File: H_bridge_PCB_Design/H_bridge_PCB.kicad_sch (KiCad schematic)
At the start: 6 parts, among them U1 ESP32-WROOM-32

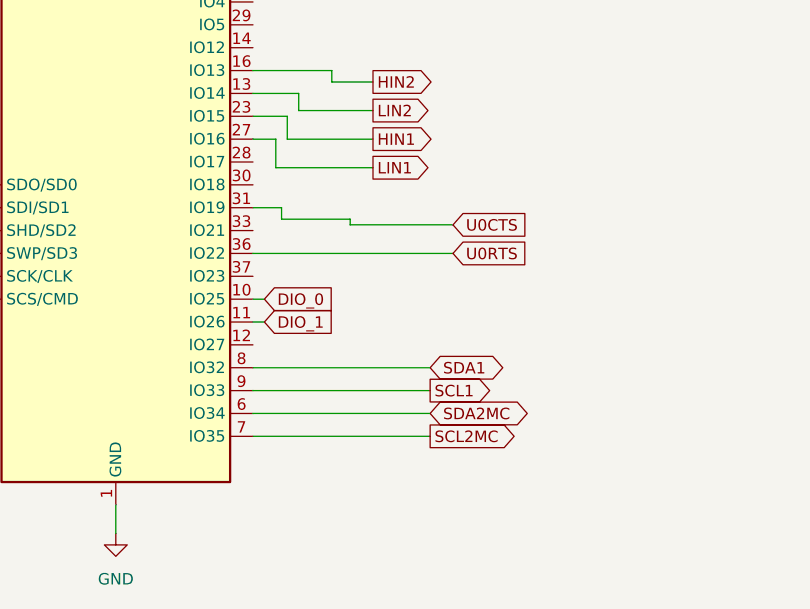
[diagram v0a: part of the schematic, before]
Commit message: Added picutres for bipolar and unipolar, changed pins for I2C-2
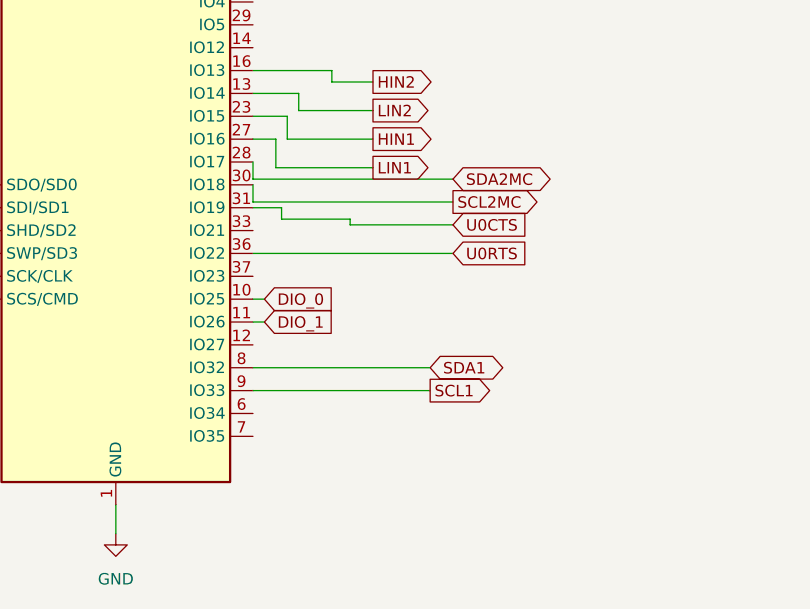
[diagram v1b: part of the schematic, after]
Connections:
- net SCL2MC: now also U1.30 (IO18); no longer U1.7 (IO35)
- net SDA2MC: now also U1.28 (IO17); no longer U1.6 (IO34)
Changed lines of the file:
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@@
+	(wire
+		(pts
+			(xy 198.12 215.9) (xy 198.12 213.995)
+		)
+		(stroke
+			(width 0)
+			(type default)
+		)
+	)
 	(wire
 		(pts
@@
 	(wire
 		(pts
-			(xy 198.12 241.935) (xy 217.805 241.935)
-		)
-		(stroke
-			(width 0)
-			(type default)
-		)
-	)
-	(wire
-		(pts
 			(xy 171.45 175.26) (xy 171.45 173.355)
 		)
@@
 	(wire
 		(pts
+			(xy 198.12 213.36) (xy 220.345 213.36)
+		)
+		(stroke
+			(width 0)
+			(type default)
+		)
+	)
+	(wire
+		(pts
 			(xy 201.93 208.915) (xy 211.455 208.915)
 		)
@@
 	(wire
 		(pts
+			(xy 220.345 215.9) (xy 198.12 215.9)
+		)
+		(stroke
+			(width 0)
+			(type default)
+		)
+	)
+	(wire
+		(pts
 			(xy 211.455 205.74) (xy 203.2 205.74)
 		)
@@
 	(wire
 		(pts
+			(xy 198.12 213.36) (xy 198.12 211.455)
+		)
+		(stroke
+			(width 0)
+			(type default)
+		)
+	)
+	(wire
+		(pts
 			(xy 213.995 187.325) (xy 206.375 187.325)
 		)
@@
 		(pts
 			(xy 211.455 202.565) (xy 206.883 202.565)
-		)
-		(stroke
-			(width 0)
-			(type default)
-		)
-	)
-	(wire
-		(pts
-			(xy 198.12 239.395) (xy 217.805 239.395)
 		)
 		(stroke
@@
 	(global_label "SCL2MC"
 		(shape output)
-		(at 217.805 241.935 0)
-		(fields_autoplaced yes)
-		(effects
-			(font
-				(size 1.27 1.27)
-			)
-			(justify left)
-		)
-		(property "Intersheetrefs" "${INTERSHEET_REFS}"
-			(at 228.2287 241.935 0)
+		(at 220.345 215.9 0)
+		(fields_autoplaced yes)
+		(effects
+			(font
+				(size 1.27 1.27)
+			)
+			(justify left)
+		)
+		(property "Intersheetrefs" "${INTERSHEET_REFS}"
+			(at 230.7687 215.9 0)
 			(effects
 				(font
@@
 	(global_label "SDA2MC"
 		(shape bidirectional)
-		(at 217.805 239.395 0)
-		(fields_autoplaced yes)
-		(effects
-			(font
-				(size 1.27 1.27)
-			)
-			(justify left)
-		)
-		(property "Intersheetrefs" "${INTERSHEET_REFS}"
-			(at 229.4005 239.395 0)
-			(effects
-				(font
+		(at 220.345 213.36 0)
+		(fields_autoplaced yes)
+		(effects
+			(font
+				(size 1.27 1.27)
+			)
+			(justify left)
+		)
+		(property "Intersheetrefs" "${INTERSHEET_REFS}"
+			(at 231.9405 213.36 0)
+			(effects
+				(font
